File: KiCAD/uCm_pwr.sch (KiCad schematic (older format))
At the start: 38 parts, among them J1 5V_EXT, J2 3V3_EXT, P13 PWR_IN, P24 PWR_IN, U3 TPS62133, U4 TPS62132

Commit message: work in progress
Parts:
- removed PCB1: PCB, PCB, symbol PCB
- C18, C20, C21, C32, C34, C35: footprint c_0805 -> uCm:c_0805
- C19, C33: footprint c_1210 -> uCm:C_1210
- C22, C26, C36, C37: footprint C_ELCO_SMD -> uCm:C_ELCO_SMD
- C30, C38: footprint c_1206 -> uCm:C_1206
- D4: footprint diode-DO214AC -> uCm:diode-DO214AC
- D5, D6, D7, D8: footprint led_0805 -> uCm:led_0805
- G1, G2: footprint Logo-WL3 -> uCm:Logo-WL3
- G3, G4: footprint OSHW_6mm -> uCm:OSHW_6mm
- J1, J2, P13: footprint Header_2 -> uCm:Header_2
- L1, L2: footprint Inductor_SMD3 -> uCm:Inductor_SMD3
- P24: footprint JACK_ALIM -> uCm:JACK_ALIM
- R10, R13, R14, R7, R8, R9: footprint r_0805 -> uCm:r_0805
- U3, U4: footprint TPS62132 -> uCm:TPS62132

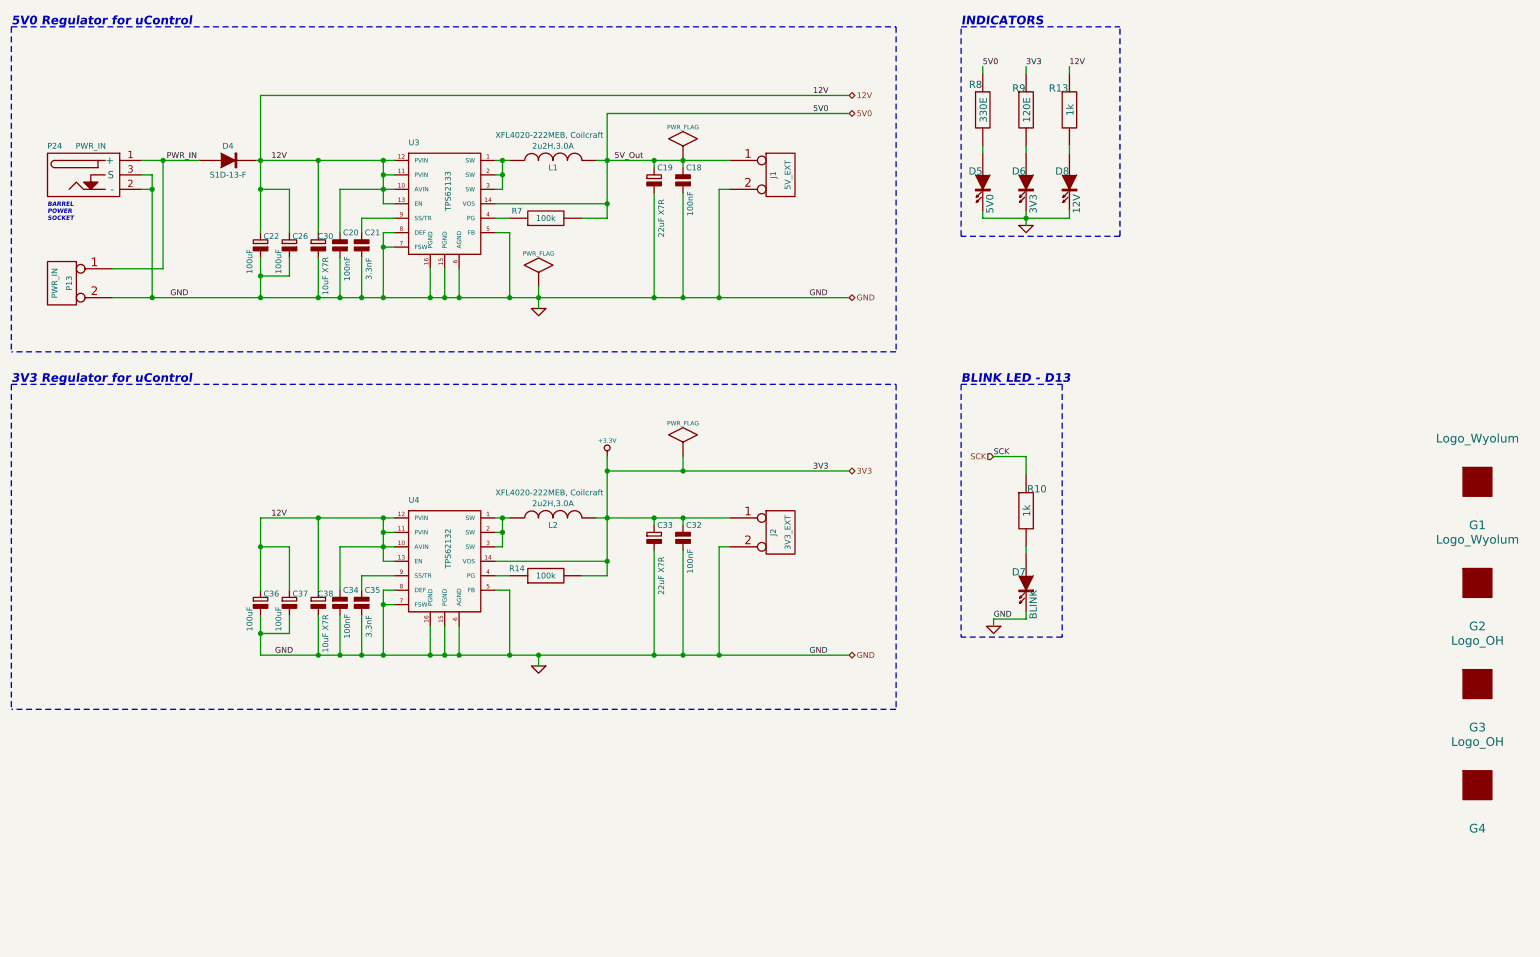
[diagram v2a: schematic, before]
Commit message: changed power supply section
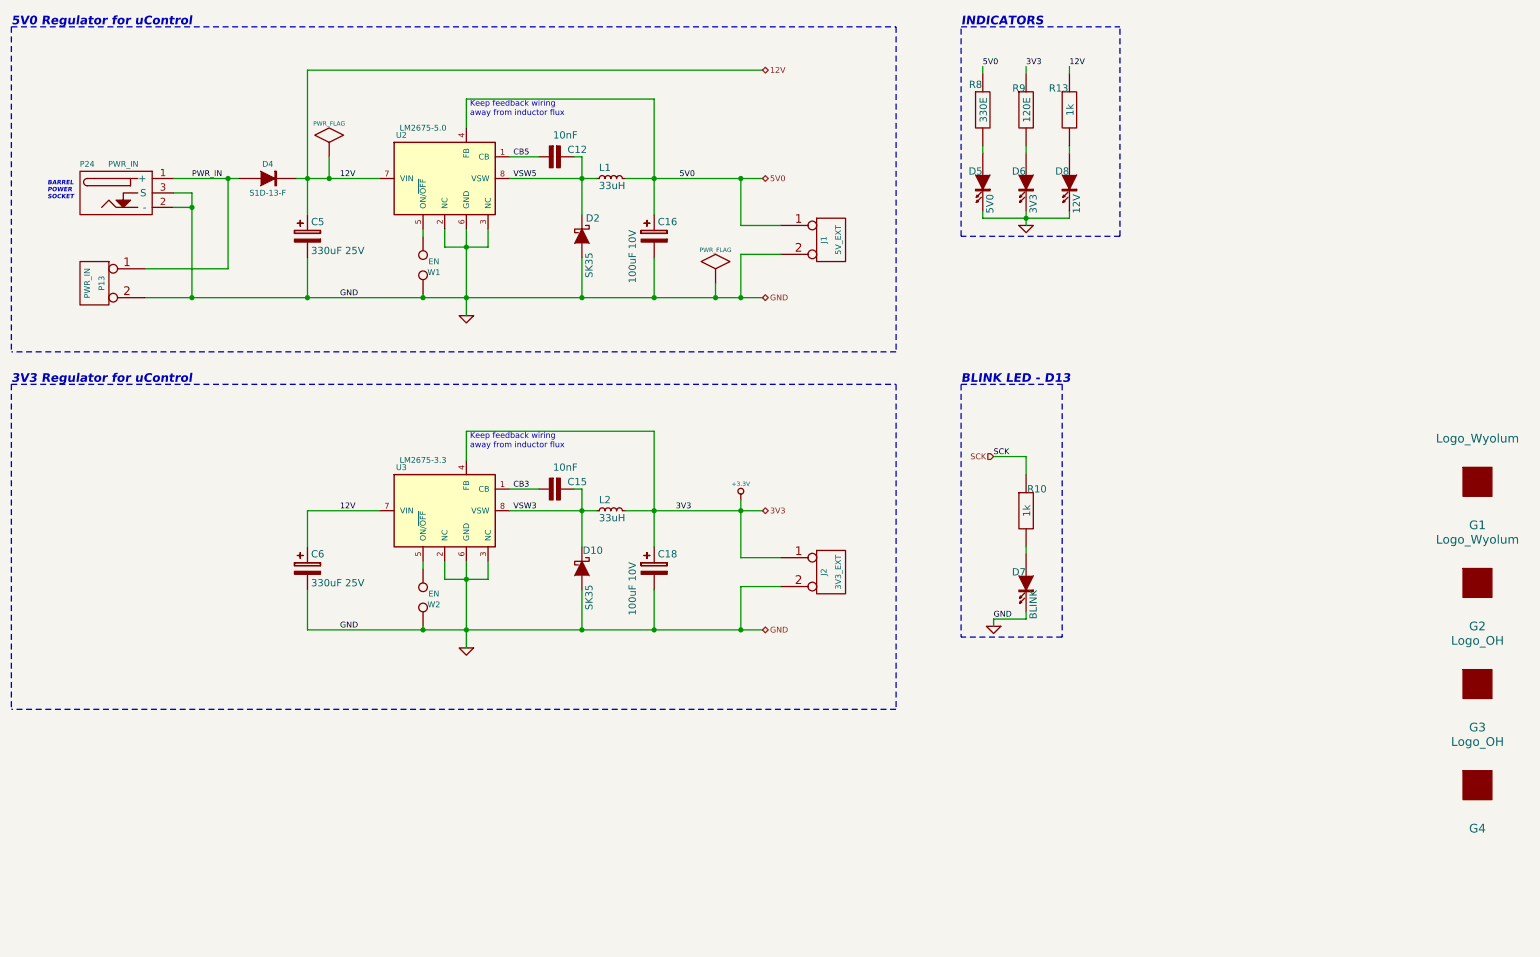
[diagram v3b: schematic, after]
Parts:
- removed C18, C20, C32, C34: 100nF, uCm:c_0805, symbol CAP_NP
- removed C19, C33: 22uF X7R, uCm:C_1210, symbol CAP_POL
- removed C21, C35: 3.3nF, uCm:c_0805, symbol CAP_NP
- removed C22, C26, C36, C37: 100uF, uCm:C_ELCO_SMD, symbol CAP_POL
- removed C30, C38: 10uF X7R, uCm:C_1206, symbol CAP_POL
- removed L1, L2: 2u2H,3.0A, uCm:Inductor_SMD3, symbol INDUCTOR
- removed R14, R7: 100k, uCm:r_0805, symbol R
- removed U3: TPS62133, uCm:TPS62132, symbol TPS62132
- removed U4: TPS62132, uCm:TPS62132, symbol TPS62132
- added C12, C15: 10nF, uCm:c_0805, symbol C
- added C16, C18: 100uF 10V, uCm:C_2917_HandSoldering, symbol CP
- added C5, C6: 330uF 25V, uCm:C_ELCO_SMD, symbol CP
- added D10, D2: SK35, uCm:Diode-SMA_Handsoldering, symbol D_Schottky
- added L1, L2: 33uH, uCm:Choke_SMD_Wuerth-WE-PD-Typ-M-Typ-S_Handsoldering, symbol L_Small
- added U2: LM2675-5.0, uCm:SO8E, symbol LM2675-5.0
- added U3: LM2675-3.3, uCm:SO8E, symbol LM2675-5.0
- added W1, W2: EN, uCm:r_0805, symbol TEST
- D4: Field10 1N4001FSCT-ND -> (none); Field11 http://www.digikey.com/product-detail/en/1N4001/1N4001FSCT-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 -> (none); Field4 DIODE GEN PURPOSE 50V 1A DO41 -> (none); Field5 50V, 1A -> (none); Field6 DO-204AL, DO-41, Axial -> (none); Field7 Fairchild Semiconductor -> (none); Field8 1N4001 -> (none); Field9 Digikey -> (none); manf# (none) -> S1D-13-F
- D5, D6, D7, D8: Field10 754-1264-ND -> (none); Field11 http://www.digikey.com/product-detail/en/WP7113ID/754-1264-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 -> (none); Field4 LED SS 5MM 625NM RED DIFF -> (none); Field5 2V, 10mA -> (none); Field6 Round with Domed Top, 5mm, T-1 3/4 -> (none); Field7 Kingbright Corp -> (none); Field8 WP7113ID -> (none); Field9 Digikey -> (none); manf# (none) -> LG M67K-H1J2-24-Z
- J1, J2, P13: manf# (none) -> PRPC002SFAN-RC
- P24: Field10 CP-002B-ND -> (none); Field11 http://www.digikey.com/product-detail/en/PJ-002B/CP-002B-ND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 -> (none); Field4 CONN POWER JACK MALE 2.5MM CLSD -> (none); Field5 Jack, Male -> (none); Field6 2.5mm ID, 5.5mm OD -> (none); Field7 CUI Inc -> (none); Field8 PJ-002B -> (none); Field9 Digikey -> (none); manf# (none) -> PJ-002B
- R10, R13: Field10 CF18JT1K00CT-ND -> (none); Field11 http://www.digikey.com/product-detail/en/CF18JT1K00/CF18JT1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 -> (none); Field4 RES 1k OHM 1/8W 5% CF AXIAL -> (none); Field5 0.125W, 1/8W -> (none); Field6 Axial -> (none); Field7 Stackpole Electronics Inc -> (none); Field8 CF18JT1K00 -> (none); Field9 Digikey -> (none); manf# (none) -> RMCF0805JT1K00
- R8: Field10 CF18JT330RCT-ND -> (none); Field11 http://www.digikey.com/product-detail/en/CF18JT330R/CF18JT3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 -> (none); Field4 RES 330 OHM 1/8W 5% CF AXIAL -> (none); Field5 0.125W, 1/8W -> (none); Field6 Axial -> (none); Field7 Stackpole Electronics Inc -> (none); Field8 CF18JT330R -> (none); Field9 Digikey -> (none); manf# (none) -> RMCF0805JT330R
- R9: Field10 CF18JT120RCT-ND -> (none); Field11 http://www.digikey.com/product-detail/en/CF18JT120R/CF18JT1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 -> (none); Field4 RES 120 OHM 1/8W 5% CF AXIAL -> (none); Field5 0.125W, 1/8W -> (none); Field6 Axial -> (none); Field7 Stackpole Electronics Inc -> (none); Field8 CF18JT120R -> (none); Field9 Digikey -> (none); manf# (none) -> RMCF0805JT120R
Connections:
- net +3.3V: now also C18.1, L2.2, U3.4 (FB)
- net 12V: now also C5.1, C6.1, U2.7 (VIN), U3.7 (VIN)
- net 5V0: now also C16.1, L1.2, U2.4 (FB)
- net GND: now also C16.2, C18.2, C5.2, C6.2, D10.1 (A), D2.1 (A), U2.2 (NC), U2.3 (NC), U2.6 (GND), U3.2 (NC), U3.3 (NC), U3.6 (GND), W1.2, W2.2
- new net: U2.5 (ON/~OFF), W1.1
- new net: U3.5 (ON/~OFF), W2.1
- new net CB3: C15.2, U3.1 (CB)
- new net CB5: C12.2, U2.1 (CB)
- new net VSW3: C15.1, D10.2 (K), L2.1, U3.8 (VSW)
- new net VSW5: C12.1, D2.2 (K), L1.1, U2.8 (VSW)
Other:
- note added: "Keep feedback wiring\naway from inductor flux"
- moved on the sheet: D4, J1, J2, P13, P24

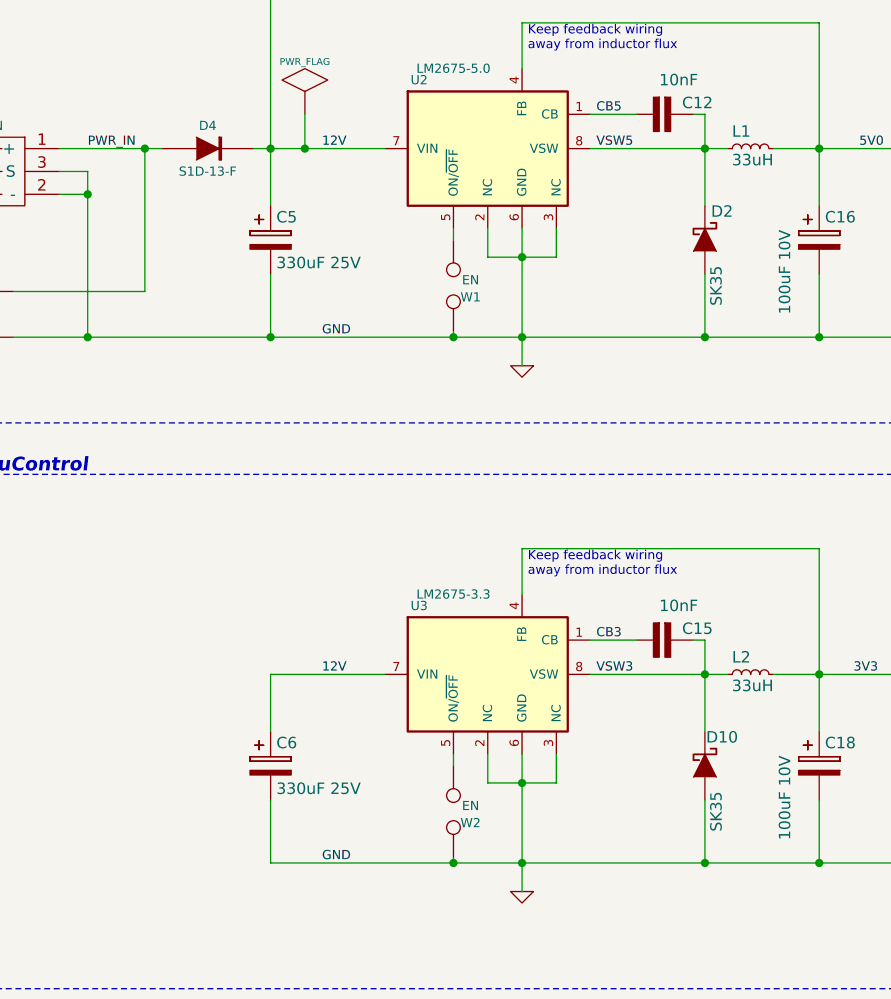
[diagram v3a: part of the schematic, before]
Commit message: changed power supply section
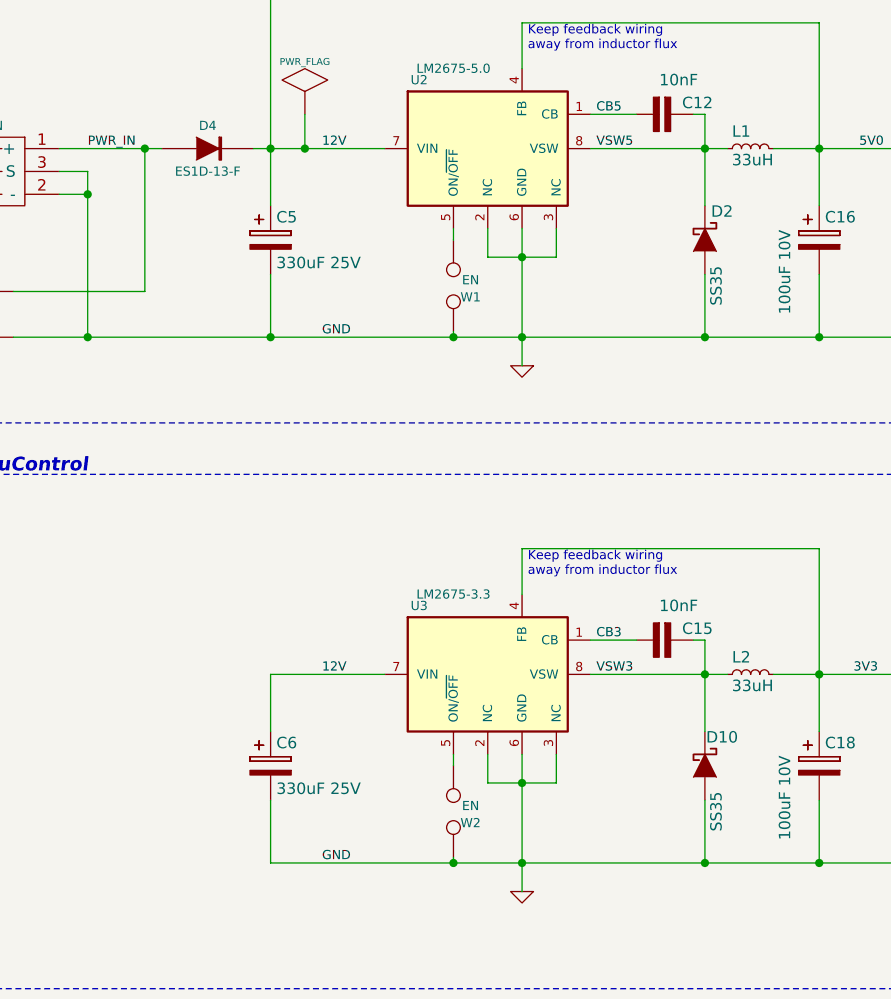
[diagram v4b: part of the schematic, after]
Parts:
- C5, C6: footprint uCm:C_ELCO_SMD -> uCm:C_ELCO_SMD_8x10
- D10, D2: value SK35 -> SS35; footprint uCm:Diode-SMA_Handsoldering -> uCm:DO-214AB; manf# SK35-7-F -> SS35
- D4: value S1D-13-F -> ES1D-13-F; footprint uCm:diode-DO214AC -> uCm:Diode-SMA; manf# S1D-13-F -> ES1D-13-F
- L1, L2: footprint uCm:Choke_SMD_Wuerth-WE-PD-Typ-M-Typ-S_Handsoldering -> uCm:Ind_Schott_330uH
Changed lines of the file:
@@
 P 2375 1650
 F 0 "D4" H 2375 1750 40  0000 C CNN
-F 1 "S1D-13-F" H 2375 1550 40  0000 C CNN
-F 2 "uCm:diode-DO214AC" H 2375 1650 40  0001 C CNN
+F 1 "ES1D-13-F" H 2375 1550 40  0000 C CNN
+F 2 "uCm:Diode-SMA" H 2375 1650 40  0001 C CNN
 F 3 "" H 2375 1650 60  0001 C CNN
-F 4 "S1D-13-F" H 2375 1650 60  0001 C CNN "manf#"
+F 4 "ES1D-13-F" H 2375 1650 60  0001 C CNN "manf#"
 	1    2375 1650
 	1    0    0    -1
@@
 P 4550 2050
 F 0 "D2" V 4425 2125 50  0000 C CNN
-F 1 "SK35" H 4750 2100 50  0000 C CNN
-F 2 "uCm:Diode-SMA_Handsoldering" H 4550 2050 60  0001 C CNN
+F 1 "SS35" H 4750 2100 50  0000 C CNN
+F 2 "uCm:DO-214AB" H 4550 2050 60  0001 C CNN
 F 3 "" H 4550 2050 60  0000 C CNN
-F 4 "SK35-7-F" V 4550 2050 60  0001 C CNN "manf#"
+F 4 "SS35" V 4550 2050 60  0001 C CNN "manf#"
 	1    4550 2050
 	0    1    1    0
@@
 F 0 "C6" H 2675 4450 50  0000 L CNN
 F 1 "330uF 25V" H 2675 4250 50  0000 L CNN
-F 2 "uCm:C_ELCO_SMD" H 2688 4200 30  0001 C CNN
+F 2 "uCm:C_ELCO_SMD_8x10" H 2688 4200 30  0001 C CNN
 F 3 "" H 2650 4350 60  0000 C CNN
 F 4 "UCL1E331MNL1GS" H 2650 4350 60  0001 C CNN "manf#"
@@
 F 0 "L2" V 4825 3950 50  0000 L CNN
 F 1 "33uH" V 4700 3850 50  0000 L CNN
-F 2 "uCm:Choke_SMD_Wuerth-WE-PD-Typ-M-Typ-S_Handsoldering" H 4750 3950 60  0001 C CNN
+F 2 "uCm:Ind_Schott_330uH" H 4750 3950 60  0001 C CNN
 F 3 "" H 4750 3950 60  0000 C CNN
 F 4 "34595" V 4750 3950 60  0001 C CNN "manf#"
@@
 P 4550 4350
 F 0 "D10" V 4425 4425 50  0000 C CNN
-F 1 "SK35" H 4750 4400 50  0000 C CNN
-F 2 "uCm:Diode-SMA_Handsoldering" H 4550 4350 60  0001 C CNN
+F 1 "SS35" H 4750 4400 50  0000 C CNN
+F 2 "uCm:DO-214AB" H 4550 4350 60  0001 C CNN
 F 3 "" H 4550 4350 60  0000 C CNN
-F 4 "SK35-7-F" V 4550 4350 60  0001 C CNN "manf#"
+F 4 "SS35" V 4550 4350 60  0001 C CNN "manf#"
 	1    4550 4350
 	0    1    1    0
@@
 F 0 "L1" V 4825 1650 50  0000 L CNN
 F 1 "33uH" V 4700 1550 50  0000 L CNN
-F 2 "uCm:Choke_SMD_Wuerth-WE-PD-Typ-M-Typ-S_Handsoldering" H 4750 1650 60  0001 C CNN
+F 2 "uCm:Ind_Schott_330uH" H 4750 1650 60  0001 C CNN
 F 3 "" H 4750 1650 60  0000 C CNN
 F 4 "34595" V 4750 1650 60  0001 C CNN "manf#"
@@
 F 0 "C5" H 2675 2150 50  0000 L CNN
 F 1 "330uF 25V" H 2675 1950 50  0000 L CNN
-F 2 "uCm:C_ELCO_SMD" H 2688 1900 30  0001 C CNN
+F 2 "uCm:C_ELCO_SMD_8x10" H 2688 1900 30  0001 C CNN
 F 3 "" H 2650 2050 60  0000 C CNN
 F 4 "UCL1E331MNL1GS" H 2650 2050 60  0001 C CNN "manf#"

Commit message: power supply sections changed
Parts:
- L1, L2: footprint uCm:Ind_Schott_330uH -> uCm:Choke_SMD_Wuerth-784775133; manf# 34595 -> 784775133
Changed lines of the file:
@@
 F 0 "L2" V 4825 3950 50  0000 L CNN
 F 1 "33uH" V 4700 3850 50  0000 L CNN
-F 2 "uCm:Ind_Schott_330uH" H 4750 3950 60  0001 C CNN
+F 2 "uCm:Choke_SMD_Wuerth-784775133" H 4750 3950 60  0001 C CNN
 F 3 "" H 4750 3950 60  0000 C CNN
-F 4 "34595" V 4750 3950 60  0001 C CNN "manf#"
+F 4 "784775133" V 4750 3950 60  0001 C CNN "manf#"
 	1    4750 3950
 	0    -1   -1   0
@@
 F 0 "L1" V 4825 1650 50  0000 L CNN
 F 1 "33uH" V 4700 1550 50  0000 L CNN
-F 2 "uCm:Ind_Schott_330uH" H 4750 1650 60  0001 C CNN
+F 2 "uCm:Choke_SMD_Wuerth-784775133" H 4750 1650 60  0001 C CNN
 F 3 "" H 4750 1650 60  0000 C CNN
-F 4 "34595" V 4750 1650 60  0001 C CNN "manf#"
+F 4 "784775133" V 4750 1650 60  0001 C CNN "manf#"
 	1    4750 1650
 	0    -1   -1   0
